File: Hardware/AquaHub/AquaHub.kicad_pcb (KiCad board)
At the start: 2 copper layers, 170 x 100 mm, 82 parts, among them J1 Screw_Terminal_01x02, J10 PinHeader6, J11 IDC_2x3, J12 IDC_2x3, J13 PinHeader2, J14 PinHeader3, J2 Screw_Terminal_01x02, J3 Screw_Terminal_01x02, J4 Screw_Terminal_01x02, J5 Screw_Terminal_01x02, J6 Screw_Terminal_01x02, J8 Screw_Terminal_01x02, J9 PinHeader3, K1 5A Relay, K2 5A Relay, K3 5A Relay, K4 5A Relay, K5 5A Relay, K6 5A Relay, Q1 BSS138, SW1 SW_Push, SW2 SW_Push, SW3 SW_Push, SW4 SW_Push, SW5 SW_Push, SW6 SW_Push, U1 ESP32-WROOM, U2 Current Sense, U3 1A 3.3V, U4 Low-Side Driver, U5 1A 5V, U6 TCA9534

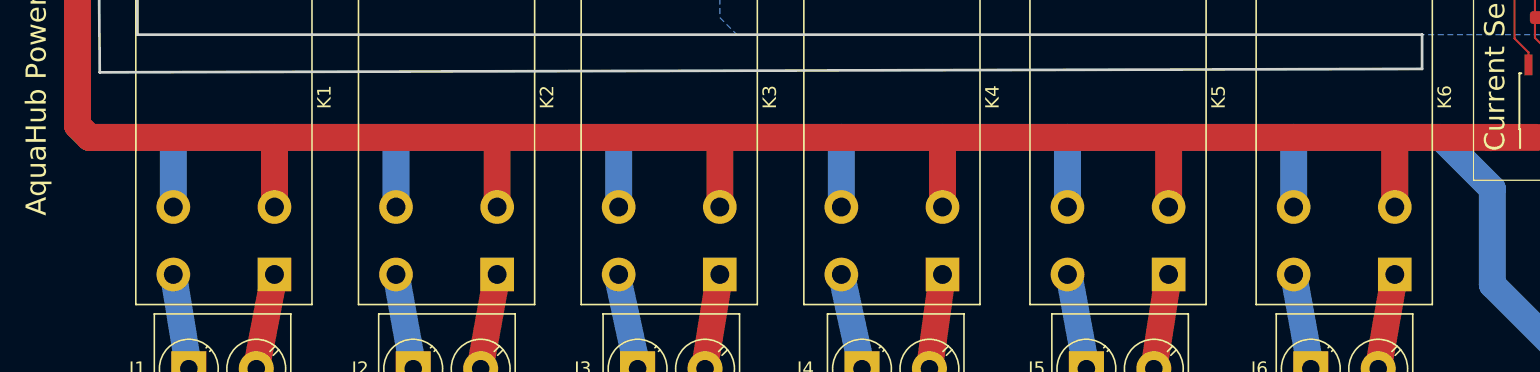
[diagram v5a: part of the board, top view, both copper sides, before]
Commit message: Updated for parts now in stdlib
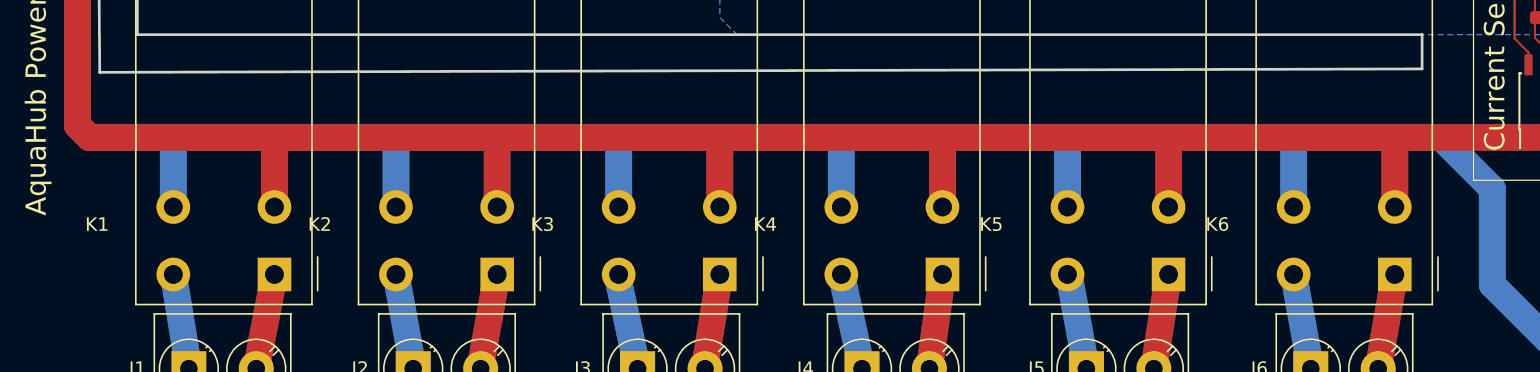
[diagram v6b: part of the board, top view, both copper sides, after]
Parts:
- turned K1 to 180 degrees
- turned K2 to 180 degrees
- turned K3 to 180 degrees
- turned K4 to 180 degrees
- turned K5 to 180 degrees
- turned K6 to 180 degrees
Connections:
- K2 pad 4: /RE2 -> (no net)

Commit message: Before trying a single-board
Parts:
- added Q2: 2SC1815, Package_TO_SOT_SMD:SOT-416, F.Cu at (195.8, 83.8)
- added R10: 1K, Resistor_SMD:R_0603_1608Metric_Pad1.05x0.95mm_HandSolder, F.Cu at (193.5, 81.4)
- added R11: 1K, Resistor_SMD:R_0603_1608Metric_Pad1.05x0.95mm_HandSolder, F.Cu at (192.9, 124.8)
- J12: footprint Connector_IDC:IDC-Header_2x03_P2.54mm_Vertical -> Connector_Molex:Molex_PicoBlade_53398-0671_1x06-1MP_P1.25mm_Vertical
- LS1: footprint Buzzer_Beeper:Buzzer_12x9.5RM7.6 -> Buzzer_Beeper:Buzzer_TDK_PS1240P02BT_D12.2mm_H6.5mm
- SW1, SW2, SW3, SW4, SW5, SW6: footprint Button_Switch_THT:SW_PUSH_6mm_H13mm -> Button_Switch_THT:SW_CK_D6R_SPST_12mm_H14.3mm
- moved SW2 5.77 mm to (117.7, 72.1), turned to 180 degrees
- moved SW3 5.77 mm to (102.7, 72.1), turned to 180 degrees
- moved SW4 5.77 mm to (87.7, 72.1), turned to 180 degrees
- moved SW5 5.77 mm to (72.7, 72.1), turned to 180 degrees
- moved SW6 5.77 mm to (57.7, 72.1), turned to 180 degrees
- moved SW1 5.77 mm to (132.7, 72.1), turned to 180 degrees
- moved RN1 2.47 mm to (147.4, 94.9)
- moved R4 2.42 mm to (194.9, 124.8), turned to 270 degrees
- moved LS1 2.16 mm to (193.0, 135.0)
- moved J12 1.88 mm to (183.6, 62.8), turned to 270 degrees
- moved D10 1.14 mm to (151.5, 95.0)
- moved D11 1.14 mm to (151.5, 96.9)
- moved D12 1.14 mm to (151.5, 98.8)
- moved D13 1.14 mm to (151.5, 100.7)
- moved D9 1.14 mm to (151.5, 93.1)
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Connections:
- K2 pad 4: (no net) -> /RE2
- LS1 pad 1: /Sounder -> +5V
- LS1 pad 2: GND -> Net-(LS1-Pad2)
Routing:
- net Net-(LS1-Pad2): track 0.00 -> 70.4 mm
- net /Sounder: track 72.2 -> 2.96 mm
- net /Panel_LED: track 140.3 -> 128.4 mm
- net GND: track 676.4 -> 666.0 mm
- net +5V: track 405.5 -> 415.1 mm, vias 0 -> 2
- net /Panel_INT: track 118.6 -> 111.8 mm
- net /Panel_SCL: track 118.0 -> 114.4 mm
- net Net-(SW1-Pad1): track 50.2 -> 46.7 mm
- net Net-(SW6-Pad1): track 116.1 -> 113.2 mm
- net Net-(Q2-Pad3): track 0.00 -> 2.65 mm
- net Net-(SW5-Pad1): track 101.1 -> 98.4 mm
- net Net-(SW4-Pad1): track 86.0 -> 83.6 mm
- net Net-(SW2-Pad1): track 64.3 -> 62.3 mm
- net /Temp_Sense: track 55.6 -> 53.9 mm
- net /RE4: track 55.4 -> 56.5 mm
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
